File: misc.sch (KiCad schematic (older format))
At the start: 16 parts

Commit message: msi2500 full pcb design
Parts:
- removed J?: USB_B, symbol USB_B
- removed U?: LP5900SDX-2.8, symbol LP5900SDX-2.8
- added J1: USB_OTG, Connectors:USB_Mini-B, symbol USB_OTG
- added U3: LP5900SDX-2.8, Housings_DFN_QFN:DFN-6-1EP_2x2mm_Pitch0.65mm, symbol LP5900SDX-2.8
- C34, C35, C36, C38, C39, C40: renamed from C?; footprint (none) -> Capacitors_SMD:C_0805
- C41, C42: renamed from C?; value C -> 10uF; footprint (none) -> Capacitors_SMD:C_0805
- D2, D3, D4: renamed from D?; footprint (none) -> Diodes_SMD:D_0805
- gave numbers to parts that had none: 3
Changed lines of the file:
@@
 EESchema Schematic File Version 2
+LIBS:msisdr-rescue
 LIBS:power
 LIBS:device
@@
 $EndDescr
 $Comp
-L USB_B J?
-U 1 1 5C690A2A
-P 7800 3700
-F 0 "J?" H 7600 4150 50  0000 L CNN
-F 1 "USB_B" H 7600 4050 50  0000 L CNN
-F 2 "" H 7950 3650 50  0001 C CNN
-F 3 "" H 7950 3650 50  0001 C CNN
-	1    7800 3700
-	-1   0    0    -1
-$EndComp
-$Comp
-L C C?
+L C C34
 U 1 1 5C690AA3
 P 4050 2900
-F 0 "C?" H 4075 3000 50  0000 L CNN
+F 0 "C34" H 4075 3000 50  0000 L CNN
 F 1 "10uF" H 4075 2800 50  0000 L CNN
-F 2 "" H 4088 2750 50  0001 C CNN
+F 2 "Capacitors_SMD:C_0805" H 4088 2750 50  0001 C CNN
 F 3 "" H 4050 2900 50  0001 C CNN
 	1    4050 2900
@@
 $EndComp
 $Comp
-L C C?
+L C C35
 U 1 1 5C690ADC
 P 4400 2900
-F 0 "C?" H 4425 3000 50  0000 L CNN
+F 0 "C35" H 4425 3000 50  0000 L CNN
 F 1 "10uF" H 4425 2800 50  0000 L CNN
-F 2 "" H 4438 2750 50  0001 C CNN
+F 2 "Capacitors_SMD:C_0805" H 4438 2750 50  0001 C CNN
 F 3 "" H 4400 2900 50  0001 C CNN
 	1    4400 2900
@@
 $EndComp
 $Comp
-L C C?
+L C C36
 U 1 1 5C690B2D
 P 4700 2900
-F 0 "C?" H 4725 3000 50  0000 L CNN
+F 0 "C36" H 4725 3000 50  0000 L CNN
 F 1 "10uF" H 4725 2800 50  0000 L CNN
-F 2 "" H 4738 2750 50  0001 C CNN
+F 2 "Capacitors_SMD:C_0805" H 4738 2750 50  0001 C CNN
 F 3 "" H 4700 2900 50  0001 C CNN
 	1    4700 2900
@@
 $EndComp
 $Comp
-L C C?
+L C C38
 U 1 1 5C690C0C
 P 5400 2900
-F 0 "C?" H 5425 3000 50  0000 L CNN
+F 0 "C38" H 5425 3000 50  0000 L CNN
 F 1 "10uF" H 5425 2800 50  0000 L CNN
-F 2 "" H 5438 2750 50  0001 C CNN
+F 2 "Capacitors_SMD:C_0805" H 5438 2750 50  0001 C CNN
 F 3 "" H 5400 2900 50  0001 C CNN
 	1    5400 2900
@@
 $EndComp
 $Comp
-L C C?
+L C C39
 U 1 1 5C690C12
 P 5750 2900
-F 0 "C?" H 5775 3000 50  0000 L CNN
+F 0 "C39" H 5775 3000 50  0000 L CNN
 F 1 "10uF" H 5775 2800 50  0000 L CNN
-F 2 "" H 5788 2750 50  0001 C CNN
+F 2 "Capacitors_SMD:C_0805" H 5788 2750 50  0001 C CNN
 F 3 "" H 5750 2900 50  0001 C CNN
 	1    5750 2900
@@
 $EndComp
 $Comp
-L C C?
+L C C40
 U 1 1 5C690C18
 P 6050 2900
-F 0 "C?" H 6075 3000 50  0000 L CNN
+F 0 "C40" H 6075 3000 50  0000 L CNN
 F 1 "10uF" H 6075 2800 50  0000 L CNN
-F 2 "" H 6088 2750 50  0001 C CNN
+F 2 "Capacitors_SMD:C_0805" H 6088 2750 50  0001 C CNN
 F 3 "" H 6050 2900 50  0001 C CNN
 	1    6050 2900
@@
 $EndComp
 $Comp
-L D D?
+L D D1
 U 1 1 5C690C27
 P 4700 3500
-F 0 "D?" H 4700 3600 50  0000 C CNN
+F 0 "D1" H 4700 3600 50  0000 C CNN
 F 1 "D" H 4700 3400 50  0000 C CNN
 F 2 "" H 4700 3500 50  0001 C CNN
@@
 $EndComp
 $Comp
-L D D?
+L D D2
 U 1 1 5C690CDD
 P 4700 3950
-F 0 "D?" H 4700 4050 50  0000 C CNN
+F 0 "D2" H 4700 4050 50  0000 C CNN
 F 1 "D" H 4700 3850 50  0000 C CNN
-F 2 "" H 4700 3950 50  0001 C CNN
+F 2 "Diodes_SMD:D_0805" H 4700 3950 50  0001 C CNN
 F 3 "" H 4700 3950 50  0001 C CNN
 	1    4700 3950
@@
 $EndComp
 $Comp
-L D D?
+L D D4
 U 1 1 5C690D30
 P 5100 4050
-F 0 "D?" H 5100 4150 50  0000 C CNN
+F 0 "D4" H 5100 4150 50  0000 C CNN
 F 1 "D" H 5100 3950 50  0000 C CNN
-F 2 "" H 5100 4050 50  0001 C CNN
+F 2 "Diodes_SMD:D_0805" H 5100 4050 50  0001 C CNN
 F 3 "" H 5100 4050 50  0001 C CNN
 	1    5100 4050
@@
 $EndComp
 $Comp
-L D D?
+L D D3
 U 1 1 5C690DBF
 P 5100 3400
-F 0 "D?" H 5100 3500 50  0000 C CNN
+F 0 "D3" H 5100 3500 50  0000 C CNN
 F 1 "D" H 5100 3300 50  0000 C CNN
-F 2 "" H 5100 3400 50  0001 C CNN
+F 2 "Diodes_SMD:D_0805" H 5100 3400 50  0001 C CNN
 F 3 "" H 5100 3400 50  0001 C CNN
 	1    5100 3400
@@
 Connection ~ 5100 3800
 $Comp
-L GND #PWR?
+L GND #PWR38
 U 1 1 5C690F71
 P 4700 4250
-F 0 "#PWR?" H 4700 4000 50  0001 C CNN
+F 0 "#PWR38" H 4700 4000 50  0001 C CNN
 F 1 "GND" H 4700 4100 50  0000 C CNN
 F 2 "" H 4700 4250 50  0001 C CNN
@@
 $EndComp
 $Comp
-L GND #PWR?
+L GND #PWR39
 U 1 1 5C690F9B
 P 5100 4300
-F 0 "#PWR?" H 5100 4050 50  0001 C CNN
+F 0 "#PWR39" H 5100 4050 50  0001 C CNN
 F 1 "GND" H 5100 4150 50  0000 C CNN
 F 2 "" H 5100 4300 50  0001 C CNN
@@
 	4200 3850 3900 3850
 $Comp
-L GND #PWR?
+L GND #PWR35
 U 1 1 5C6911FA
 P 4050 3150
-F 0 "#PWR?" H 4050 2900 50  0001 C CNN
+F 0 "#PWR35" H 4050 2900 50  0001 C CNN
 F 1 "GND" H 4050 3000 50  0000 C CNN
 F 2 "" H 4050 3150 50  0001 C CNN
@@
 $EndComp
 $Comp
-L GND #PWR?
+L GND #PWR36
 U 1 1 5C691224
 P 4400 3150
-F 0 "#PWR?" H 4400 2900 50  0001 C CNN
+F 0 "#PWR36" H 4400 2900 50  0001 C CNN
 F 1 "GND" H 4400 3000 50  0000 C CNN
 F 2 "" H 4400 3150 50  0001 C CNN
@@
 $EndComp
 $Comp
-L GND #PWR?
+L GND #PWR37
 U 1 1 5C69124E
 P 4700 3150
-F 0 "#PWR?" H 4700 2900 50  0001 C CNN
+F 0 "#PWR37" H 4700 2900 50  0001 C CNN
 F 1 "GND" H 4700 3000 50  0000 C CNN
 F 2 "" H 4700 3150 50  0001 C CNN
@@
 $EndComp
 $Comp
-L GND #PWR?
+L GND #PWR41
 U 1 1 5C691278
 P 5400 3150
-F 0 "#PWR?" H 5400 2900 50  0001 C CNN
+F 0 "#PWR41" H 5400 2900 50  0001 C CNN
 F 1 "GND" H 5400 3000 50  0000 C CNN
 F 2 "" H 5400 3150 50  0001 C CNN
@@
 $EndComp
 $Comp
-L GND #PWR?
+L GND #PWR42
 U 1 1 5C6912A2
 P 5750 3150
-F 0 "#PWR?" H 5750 2900 50  0001 C CNN
+F 0 "#PWR42" H 5750 2900 50  0001 C CNN
 F 1 "GND" H 5750 3000 50  0000 C CNN
 F 2 "" H 5750 3150 50  0001 C CNN
@@
 $EndComp
 $Comp
-L GND #PWR?
+L GND #PWR44
 U 1 1 5C6912CC
 P 6050 3150
-F 0 "#PWR?" H 6050 2900 50  0001 C CNN
+F 0 "#PWR44" H 6050 2900 50  0001 C CNN
 F 1 "GND" H 6050 3000 50  0000 C CNN
 F 2 "" H 6050 3150 50  0001 C CNN
@@
 	4050 3150 4050 3050
 $Comp
-L AP2204R-3.0 U?
+L AP2204R-3.0 U4
 U 1 1 5C691501
 P 6800 2550
-F 0 "U?" H 6600 2675 50  0000 L CNN
+F 0 "U4" H 6600 2675 50  0000 L CNN
 F 1 "AP7313-30SAG" H 6800 2675 50  0000 L CNN
 F 2 "TO_SOT_Packages_SMD:SOT-89-3" H 6800 2775 50  0001 C CNN
@@
 $EndComp
 $Comp
-L C C?
+L C C42
 U 1 1 5C691852
 P 7150 3000
-F 0 "C?" H 7175 3100 50  0000 L CNN
-F 1 "C" H 7175 2900 50  0000 L CNN
-F 2 "" H 7188 2850 50  0001 C CNN
+F 0 "C42" H 7175 3100 50  0000 L CNN
+F 1 "10uF" H 7175 2900 50  0000 L CNN
+F 2 "Capacitors_SMD:C_0805" H 7188 2850 50  0001 C CNN
 F 3 "" H 7150 3000 50  0001 C CNN
 	1    7150 3000
@@
 $EndComp
 $Comp
-L C C?
+L C C41
 U 1 1 5C6918BB
 P 6450 2950
-F 0 "C?" H 6475 3050 50  0000 L CNN
-F 1 "C" H 6475 2850 50  0000 L CNN
-F 2 "" H 6488 2800 50  0001 C CNN
+F 0 "C41" H 6475 3050 50  0000 L CNN
+F 1 "10uF" H 6475 2850 50  0000 L CNN
+F 2 "Capacitors_SMD:C_0805" H 6488 2800 50  0001 C CNN
 F 3 "" H 6450 2950 50  0001 C CNN
 	1    6450 2950
@@
 	7150 2550 7150 2850
 $Comp
-L GND #PWR?
+L GND #PWR46
 U 1 1 5C691B40
 P 6800 3250
-F 0 "#PWR?" H 6800 3000 50  0001 C CNN
+F 0 "#PWR46" H 6800 3000 50  0001 C CNN
 F 1 "GND" H 6800 3100 50  0000 C CNN
 F 2 "" H 6800 3250 50  0001 C CNN
@@
 Connection ~ 6050 2650
 Connection ~ 6450 2550
-$Comp
-L LP5900SDX-2.8 U?
-U 1 1 5C691E4C
-P 5850 1450
-F 0 "U?" H 5850 1450 60  0000 C CNN
-F 1 "LP5900SDX-2.8" H 6200 1250 31  0000 C CNN
-F 2 "" H 5850 1450 60  0001 C CNN
-F 3 "" H 5850 1450 60  0001 C CNN
-	1    5850 1450
-	1    0    0    -1
-$EndComp
 Wire Wire Line
 	7450 3500 7500 3500
@@
 Connection ~ 7150 2550
 $Comp
-L GND #PWR?
+L GND #PWR45
 U 1 1 5C692086
 P 6450 3200
-F 0 "#PWR?" H 6450 2950 50  0001 C CNN
+F 0 "#PWR45" H 6450 2950 50  0001 C CNN
 F 1 "GND" H 6450 3050 50  0000 C CNN
 F 2 "" H 6450 3200 50  0001 C CNN
@@
 $EndComp
 $Comp
-L GND #PWR?
+L GND #PWR47
 U 1 1 5C6920B8
 P 7150 3250
-F 0 "#PWR?" H 7150 3000 50  0001 C CNN
+F 0 "#PWR47" H 7150 3000 50  0001 C CNN
 F 1 "GND" H 7150 3100 50  0000 C CNN
 F 2 "" H 7150 3250 50  0001 C CNN
@@
 	7150 3250 7150 3150
 $Comp
-L GND #PWR?
+L GND #PWR43
 U 1 1 5C69221A
 P 6050 2200
-F 0 "#PWR?" H 6050 1950 50  0001 C CNN
+F 0 "#PWR43" H 6050 1950 50  0001 C CNN
 F 1 "GND" H 6050 2050 50  0000 C CNN
 F 2 "" H 6050 2200 50  0001 C CNN
@@
 NoConn ~ 5650 1750
 $Comp
-L C C?
+L C C37
 U 1 1 5C69264E
 P 5350 1900
-F 0 "C?" H 5375 2000 50  0000 L CNN
+F 0 "C37" H 5375 2000 50  0000 L CNN
 F 1 "10uF" H 5375 1800 50  0000 L CNN
 F 2 "" H 5388 1750 50  0001 C CNN
@@
 Connection ~ 5350 1500
 $Comp
-L GND #PWR?
+L GND #PWR40
 U 1 1 5C692712
 P 5350 2200
-F 0 "#PWR?" H 5350 1950 50  0001 C CNN
+F 0 "#PWR40" H 5350 1950 50  0001 C CNN
 F 1 "GND" H 5350 2050 50  0000 C CNN
 F 2 "" H 5350 2200 50  0001 C CNN
@@
 	6050 2100 6050 2200
 $Comp
-L GND #PWR?
+L GND #PWR48
 U 1 1 5C693D92
 P 7800 4300
-F 0 "#PWR?" H 7800 4050 50  0001 C CNN
+F 0 "#PWR48" H 7800 4050 50  0001 C CNN
 F 1 "GND" H 7800 4150 50  0000 C CNN
 F 2 "" H 7800 4300 50  0001 C CNN
@@
 Wire Wire Line
 	7800 4300 7800 4100
+$Comp
+L USB_OTG J1
+U 1 1 5C695F80
+P 7800 3700
+F 0 "J1" H 7600 4150 50  0000 L CNN
+F 1 "USB_OTG" H 7600 4050 50  0000 L CNN
+F 2 "Connectors:USB_Mini-B" H 7950 3650 50  0001 C CNN
+F 3 "" H 7950 3650 50  0001 C CNN
+	1    7800 3700
+	-1   0    0    -1
+$EndComp
+$Comp
+L LP5900SDX-2.8 U3
+U 1 1 5C6992EB
+P 5850 1450
+F 0 "U3" H 5850 1450 60  0000 C CNN
+F 1 "LP5900SDX-2.8" H 6200 1250 31  0000 C CNN
+F 2 "Housings_DFN_QFN:DFN-6-1EP_2x2mm_Pitch0.65mm" H 5850 1450 60  0001 C CNN
+F 3 "" H 5850 1450 60  0001 C CNN
+	1    5850 1450
+	1    0    0    -1
+$EndComp
 $EndSCHEMATC

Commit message: update and fix bug
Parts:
- removed C34, C35, C36, C38, C39, C40: 10uF, Capacitors_SMD:C_0805, symbol C
- added C35: 100uF, Capacitors_THT:CP_Radial_D5.0mm_P2.50mm, symbol CP
- C36: renamed from C37; footprint (none) -> Capacitors_SMD:C_0805
- D1: footprint (none) -> Diodes_SMD:D_0805
- renumbered C41 to C37, C42 to C38, J1 to J11
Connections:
- net GND: now also C35.2
- net VDIG: now also C35.1
- no-connect marks 2 -> 4
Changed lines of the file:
@@
 $EndDescr
-$Comp
-L C C34
-U 1 1 5C690AA3
-P 4050 2900
-F 0 "C34" H 4075 3000 50  0000 L CNN
-F 1 "10uF" H 4075 2800 50  0000 L CNN
-F 2 "Capacitors_SMD:C_0805" H 4088 2750 50  0001 C CNN
-F 3 "" H 4050 2900 50  0001 C CNN
-	1    4050 2900
-	1    0    0    -1
-$EndComp
-$Comp
-L C C35
-U 1 1 5C690ADC
-P 4400 2900
-F 0 "C35" H 4425 3000 50  0000 L CNN
-F 1 "10uF" H 4425 2800 50  0000 L CNN
-F 2 "Capacitors_SMD:C_0805" H 4438 2750 50  0001 C CNN
-F 3 "" H 4400 2900 50  0001 C CNN
-	1    4400 2900
-	1    0    0    -1
-$EndComp
-$Comp
-L C C36
-U 1 1 5C690B2D
-P 4700 2900
-F 0 "C36" H 4725 3000 50  0000 L CNN
-F 1 "10uF" H 4725 2800 50  0000 L CNN
-F 2 "Capacitors_SMD:C_0805" H 4738 2750 50  0001 C CNN
-F 3 "" H 4700 2900 50  0001 C CNN
-	1    4700 2900
-	1    0    0    -1
-$EndComp
-$Comp
-L C C38
-U 1 1 5C690C0C
-P 5400 2900
-F 0 "C38" H 5425 3000 50  0000 L CNN
-F 1 "10uF" H 5425 2800 50  0000 L CNN
-F 2 "Capacitors_SMD:C_0805" H 5438 2750 50  0001 C CNN
-F 3 "" H 5400 2900 50  0001 C CNN
-	1    5400 2900
-	1    0    0    -1
-$EndComp
-$Comp
-L C C39
-U 1 1 5C690C12
-P 5750 2900
-F 0 "C39" H 5775 3000 50  0000 L CNN
-F 1 "10uF" H 5775 2800 50  0000 L CNN
-F 2 "Capacitors_SMD:C_0805" H 5788 2750 50  0001 C CNN
-F 3 "" H 5750 2900 50  0001 C CNN
-	1    5750 2900
-	1    0    0    -1
-$EndComp
-$Comp
-L C C40
-U 1 1 5C690C18
-P 6050 2900
-F 0 "C40" H 6075 3000 50  0000 L CNN
-F 1 "10uF" H 6075 2800 50  0000 L CNN
-F 2 "Capacitors_SMD:C_0805" H 6088 2750 50  0001 C CNN
-F 3 "" H 6050 2900 50  0001 C CNN
-	1    6050 2900
-	1    0    0    -1
-$EndComp
 $Comp
 L D D1
@@
 F 0 "D1" H 4700 3600 50  0000 C CNN
 F 1 "D" H 4700 3400 50  0000 C CNN
-F 2 "" H 4700 3500 50  0001 C CNN
+F 2 "Diodes_SMD:D_0805" H 4700 3500 50  0001 C CNN
 F 3 "" H 4700 3500 50  0001 C CNN
 	1    4700 3500
@@
 $EndComp
 Wire Wire Line
-	4050 2750 4050 2650
-Wire Wire Line
-	4050 2650 6250 2650
-Wire Wire Line
-	6050 2650 6050 2750
-Wire Wire Line
-	5750 2750 5750 2650
-Connection ~ 5750 2650
-Wire Wire Line
-	5400 2750 5400 2650
-Connection ~ 5400 2650
-Wire Wire Line
-	4700 2750 4700 2650
-Connection ~ 4700 2650
-Wire Wire Line
-	4400 2750 4400 2650
-Connection ~ 4400 2650
+	4600 2650 6250 2650
 Wire Wire Line
 	5100 3250 5100 2650
@@
 Connection ~ 5100 3800
 $Comp
-L GND #PWR38
+L GND #PWR36
 U 1 1 5C690F71
 P 4700 4250
-F 0 "#PWR38" H 4700 4000 50  0001 C CNN
+F 0 "#PWR36" H 4700 4000 50  0001 C CNN
 F 1 "GND" H 4700 4100 50  0000 C CNN
 F 2 "" H 4700 4250 50  0001 C CNN
@@
 $EndComp
 $Comp
-L GND #PWR39
+L GND #PWR37
 U 1 1 5C690F9B
 P 5100 4300
-F 0 "#PWR39" H 5100 4050 50  0001 C CNN
+F 0 "#PWR37" H 5100 4050 50  0001 C CNN
 F 1 "GND" H 5100 4150 50  0000 C CNN
 F 2 "" H 5100 4300 50  0001 C CNN
@@
 Wire Wire Line
 	4950 3350 4950 2650
-Connection ~ 4950 2650
-Text GLabel 4250 2250 0    20   Output ~ 0
+Text GLabel 4250 2250 0    20   Input ~ 0
 VDIG
 Wire Wire Line
@@
 	5200 2250 5200 2650
 Connection ~ 5200 2650
-Text GLabel 3900 3850 0    20   BiDi ~ 0
+Text GLabel 3900 3850 0    20   Input ~ 0
 USB_DM
-Text GLabel 3900 3600 0    20   BiDi ~ 0
+Text GLabel 3900 3600 0    20   Input ~ 0
 USB_DP
 Wire Wire Line
@@
 L GND #PWR35
 U 1 1 5C6911FA
-P 4050 3150
-F 0 "#PWR35" H 4050 2900 50  0001 C CNN
-F 1 "GND" H 4050 3000 50  0000 C CNN
-F 2 "" H 4050 3150 50  0001 C CNN
-F 3 "" H 4050 3150 50  0001 C CNN
-	1    4050 3150
-	1    0    0    -1
-$EndComp
-$Comp
-L GND #PWR36
-U 1 1 5C691224
-P 4400 3150
-F 0 "#PWR36" H 4400 2900 50  0001 C CNN
-F 1 "GND" H 4400 3000 50  0000 C CNN
-F 2 "" H 4400 3150 50  0001 C CNN
-F 3 "" H 4400 3150 50  0001 C CNN
-	1    4400 3150
-	1    0    0    -1
-$EndComp
-$Comp
-L GND #PWR37
-U 1 1 5C69124E
-P 4700 3150
-F 0 "#PWR37" H 4700 2900 50  0001 C CNN
-F 1 "GND" H 4700 3000 50  0000 C CNN
-F 2 "" H 4700 3150 50  0001 C CNN
-F 3 "" H 4700 3150 50  0001 C CNN
-	1    4700 3150
-	1    0    0    -1
-$EndComp
-$Comp
-L GND #PWR41
-U 1 1 5C691278
-P 5400 3150
-F 0 "#PWR41" H 5400 2900 50  0001 C CNN
-F 1 "GND" H 5400 3000 50  0000 C CNN
-F 2 "" H 5400 3150 50  0001 C CNN
-F 3 "" H 5400 3150 50  0001 C CNN
-	1    5400 3150
-	1    0    0    -1
-$EndComp
-$Comp
-L GND #PWR42
-U 1 1 5C6912A2
-P 5750 3150
-F 0 "#PWR42" H 5750 2900 50  0001 C CNN
-F 1 "GND" H 5750 3000 50  0000 C CNN
-F 2 "" H 5750 3150 50  0001 C CNN
-F 3 "" H 5750 3150 50  0001 C CNN
-	1    5750 3150
-	1    0    0    -1
-$EndComp
-$Comp
-L GND #PWR44
-U 1 1 5C6912CC
-P 6050 3150
-F 0 "#PWR44" H 6050 2900 50  0001 C CNN
-F 1 "GND" H 6050 3000 50  0000 C CNN
-F 2 "" H 6050 3150 50  0001 C CNN
-F 3 "" H 6050 3150 50  0001 C CNN
-	1    6050 3150
-	1    0    0    -1
-$EndComp
-Wire Wire Line
-	6050 3150 6050 3050
-Wire Wire Line
-	5750 3150 5750 3050
-Wire Wire Line
-	5400 3150 5400 3050
-Wire Wire Line
-	4700 3150 4700 3050
-Wire Wire Line
-	4400 3150 4400 3050
-Wire Wire Line
-	4050 3150 4050 3050
+P 4600 3200
+F 0 "#PWR35" H 4600 2950 50  0001 C CNN
+F 1 "GND" H 4600 3050 50  0000 C CNN
+F 2 "" H 4600 3200 50  0001 C CNN
+F 3 "" H 4600 3200 50  0001 C CNN
+	1    4600 3200
+	1    0    0    -1
+$EndComp
 $Comp
 L AP2204R-3.0 U4
@@
 $EndComp
 $Comp
-L C C42
+L C C38
 U 1 1 5C691852
 P 7150 3000
-F 0 "C42" H 7175 3100 50  0000 L CNN
+F 0 "C38" H 7175 3100 50  0000 L CNN
 F 1 "10uF" H 7175 2900 50  0000 L CNN
 F 2 "Capacitors_SMD:C_0805" H 7188 2850 50  0001 C CNN
@@
 $EndComp
 $Comp
-L C C41
+L C C37
 U 1 1 5C6918BB
 P 6450 2950
-F 0 "C41" H 6475 3050 50  0000 L CNN
+F 0 "C37" H 6475 3050 50  0000 L CNN
 F 1 "10uF" H 6475 2850 50  0000 L CNN
 F 2 "Capacitors_SMD:C_0805" H 6488 2800 50  0001 C CNN
@@
 	7150 2550 7150 2850
 $Comp
-L GND #PWR46
+L GND #PWR41
 U 1 1 5C691B40
 P 6800 3250
-F 0 "#PWR46" H 6800 3000 50  0001 C CNN
+F 0 "#PWR41" H 6800 3000 50  0001 C CNN
 F 1 "GND" H 6800 3100 50  0000 C CNN
 F 2 "" H 6800 3250 50  0001 C CNN
@@
 Wire Wire Line
 	6250 2650 6250 2550
-Connection ~ 6050 2650
 Connection ~ 6450 2550
-Wire Wire Line
-	7450 3500 7500 3500
 Wire Wire Line
 	7450 1550 7450 3500
 Connection ~ 7150 2550
 $Comp
-L GND #PWR45
+L GND #PWR40
 U 1 1 5C692086
 P 6450 3200
-F 0 "#PWR45" H 6450 2950 50  0001 C CNN
+F 0 "#PWR40" H 6450 2950 50  0001 C CNN
 F 1 "GND" H 6450 3050 50  0000 C CNN
 F 2 "" H 6450 3200 50  0001 C CNN
@@
 $EndComp
 $Comp
-L GND #PWR47
+L GND #PWR42
 U 1 1 5C6920B8
 P 7150 3250
-F 0 "#PWR47" H 7150 3000 50  0001 C CNN
+F 0 "#PWR42" H 7150 3000 50  0001 C CNN
 F 1 "GND" H 7150 3100 50  0000 C CNN
 F 2 "" H 7150 3250 50  0001 C CNN
@@
 	7150 3250 7150 3150
 $Comp
-L GND #PWR43
+L GND #PWR39
 U 1 1 5C69221A
 P 6050 2200
-F 0 "#PWR43" H 6050 1950 50  0001 C CNN
+F 0 "#PWR39" H 6050 1950 50  0001 C CNN
 F 1 "GND" H 6050 2050 50  0000 C CNN
 F 2 "" H 6050 2200 50  0001 C CNN
@@
 	1    0    0    -1
 $EndComp
-Text GLabel 5150 1500 0    24   Output ~ 0
+Text GLabel 5150 1500 0    24   Input ~ 0
 VRF
 Wire Wire Line
@@
 NoConn ~ 5650 1750
 $Comp
-L C C37
+L C C36
 U 1 1 5C69264E
 P 5350 1900
-F 0 "C37" H 5375 2000 50  0000 L CNN
+F 0 "C36" H 5375 2000 50  0000 L CNN
 F 1 "10uF" H 5375 1800 50  0000 L CNN
-F 2 "" H 5388 1750 50  0001 C CNN
+F 2 "Capacitors_SMD:C_0805" H 5388 1750 50  0001 C CNN
 F 3 "" H 5350 1900 50  0001 C CNN
 	1    5350 1900
@@
 Connection ~ 5350 1500
 $Comp
-L GND #PWR40
+L GND #PWR38
 U 1 1 5C692712
 P 5350 2200
-F 0 "#PWR40" H 5350 1950 50  0001 C CNN
+F 0 "#PWR38" H 5350 1950 50  0001 C CNN
 F 1 "GND" H 5350 2050 50  0000 C CNN
 F 2 "" H 5350 2200 50  0001 C CNN
@@
 	6050 2100 6050 2200
 $Comp
-L GND #PWR48
+L GND #PWR43
 U 1 1 5C693D92
 P 7800 4300
-F 0 "#PWR48" H 7800 4050 50  0001 C CNN
+F 0 "#PWR43" H 7800 4050 50  0001 C CNN
 F 1 "GND" H 7800 4150 50  0000 C CNN
 F 2 "" H 7800 4300 50  0001 C CNN
@@
 	7800 4300 7800 4100
 $Comp
-L USB_OTG J1
+L USB_OTG J11
 U 1 1 5C695F80
 P 7800 3700
-F 0 "J1" H 7600 4150 50  0000 L CNN
+F 0 "J11" H 7600 4150 50  0000 L CNN
 F 1 "USB_OTG" H 7600 4050 50  0000 L CNN
 F 2 "Connectors:USB_Mini-B" H 7950 3650 50  0001 C CNN
@@
 	1    0    0    -1
 $EndComp
+NoConn ~ 7500 3900
+NoConn ~ 7900 4100
+Wire Wire Line
+	7450 3500 7500 3500
+Wire Wire Line
+	4600 2650 4600 2800
+Connection ~ 4950 2650
+$Comp
+L CP C35
+U 1 1 5C6ADA0A
+P 4600 2950
+F 0 "C35" H 4625 3050 50  0000 L CNN
+F 1 "100uF" H 4625 2850 50  0000 L CNN
+F 2 "Capacitors_THT:CP_Radial_D5.0mm_P2.50mm" H 4638 2800 50  0001 C CNN
+F 3 "" H 4600 2950 50  0001 C CNN
+	1    4600 2950
+	1    0    0    -1
+$EndComp
+Wire Wire Line
+	4600 3200 4600 3100
 $EndSCHEMATC

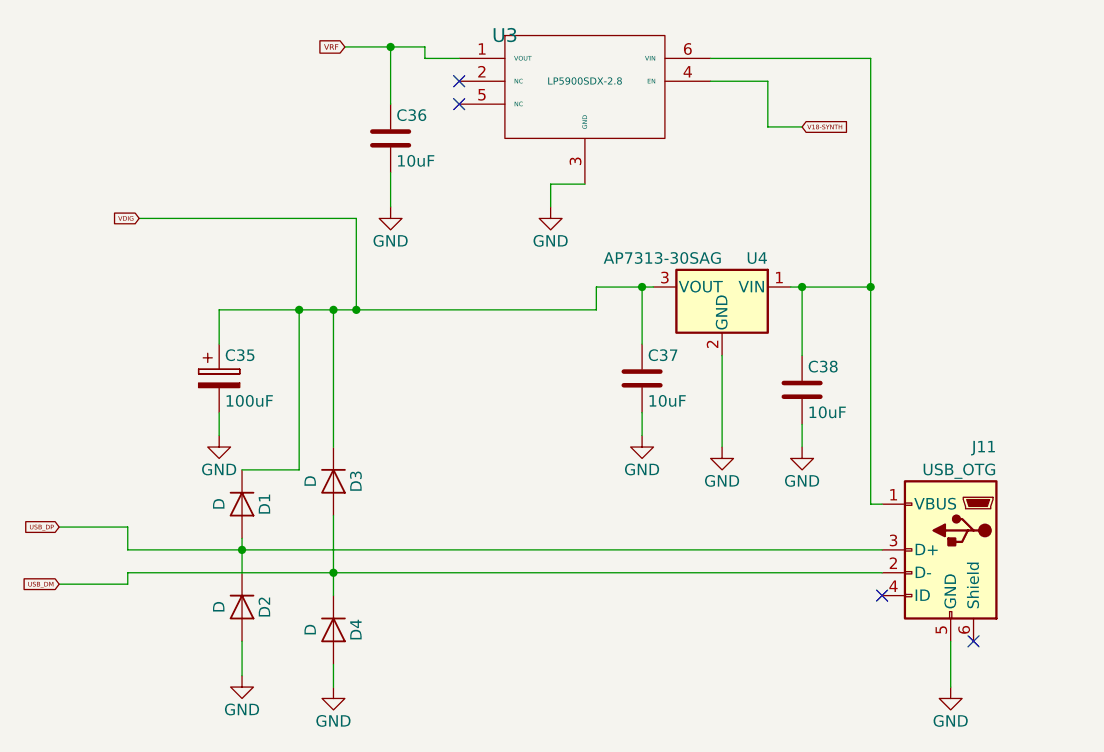
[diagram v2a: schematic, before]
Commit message: change ldo to ap2204r
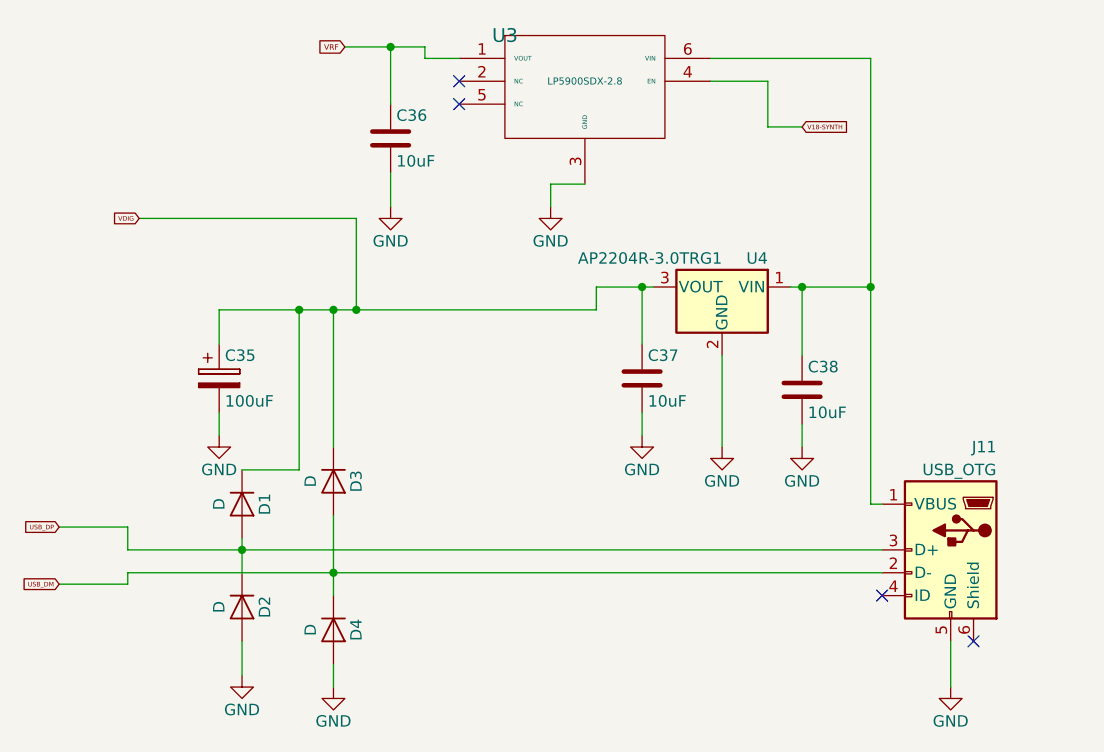
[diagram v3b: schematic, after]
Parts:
- U4: value AP7313-30SAG -> AP2204R-3.0TRG1
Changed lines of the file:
@@
 P 6800 2550
 F 0 "U4" H 6600 2675 50  0000 L CNN
-F 1 "AP7313-30SAG" H 6800 2675 50  0000 L CNN
+F 1 "AP2204R-3.0TRG1" H 6800 2675 50  0000 L CNN
 F 2 "TO_SOT_Packages_SMD:SOT-89-3" H 6800 2775 50  0001 C CNN
 F 3 "" H 6800 2550 50  0001 C CNN
